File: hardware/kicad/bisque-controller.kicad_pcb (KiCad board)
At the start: 2 copper layers, 100 x 80 mm, 52 parts, among them J1 USB-C, J2 5V_IN, J3 TC_K, J4 SSR, J5 DISPLAY, J6 NAV_SW, J7 AUX, Q1 AO3400A, Q2 AO3400A, SW1 RESET, SW2 BOOT, U1 ESP32-S3-WROOM-1-N16R8, U2 AMS1117-3.3, U3 MAX31855KASA+, U4 USBLC6-2SC6

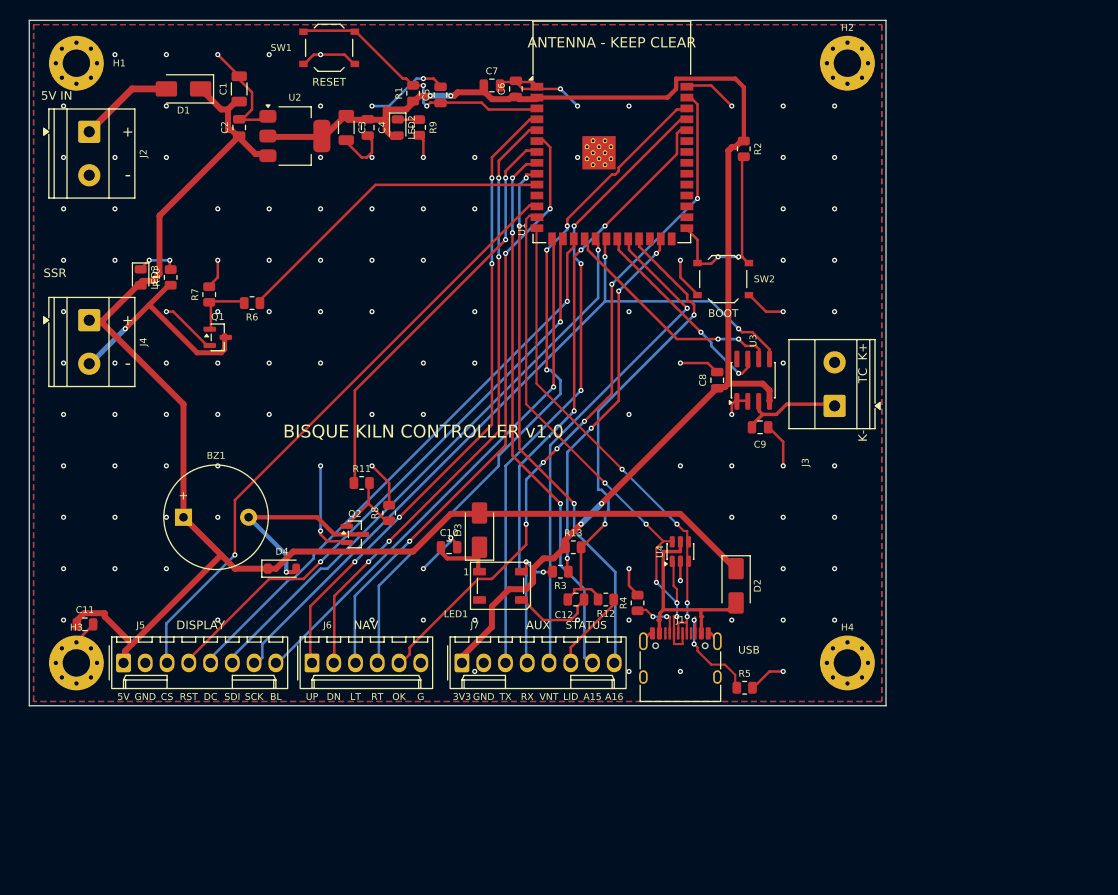
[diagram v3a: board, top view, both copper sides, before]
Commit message: wip(hw): rev B place and route — rung 2, still 27 unconnected
Full re-placement of all 141 footprints and a first end-to-end route of the
rev B board. Does NOT reach the 0-error/0-unconnected gate: 78 DRC violations,
27 unconnected pads, 9 nets the router could not finish. Spec 6.3's ladder was
worked in order and neither affordable rung closed it.

  rung 0 (100x100, 0805): 34 unroutable, 149 violations, 38 unconnected
  rung 1 (100x100, 0603): 23 unroutable,  84 violations, 32 unconnected
  rung 2 (125x100, 0603):  9 unroutable,  78 violations, 27 unconnected

Rung 3 (4-layer) is what the remaining failures point at — they are all short
local nets boxed in by neighbours' copper, i.e. short of routing layer, not of
board area — but that changes the stack-up and fab cost, so it is escalated
rather than started. See .superpowers/sdd/2026-08-11-pcb-rev-b/task-14-report.md.

Placement is now data, not 141 hand-typed coordinates: floorplan.py holds the
region rectangles, the pinned parts and a seed per part plus an overlap
legalizer; apply_floorplan.py writes the result into design.py; and
check_placement.py answers "does anything collide" from design.py in a second
instead of after a 20-minute route and fill. Final: 0 courtyard overlaps,
0 parts off-board.

Generator fixes this needed, none of which relax a rule:

- kicad_build.py had never been run. It crashed in add_zones (pcbnew.LSET
  takes no python list in KiCad 10) and its ref-relocation table still named
  C9, deleted with the MAX31855.
- Dropped the WROOM-1 antenna keepout fallback. The 1U has no PCB antenna;
  inventing a keep-out for it barred tracks from a third of the digital band
  and forfeited the band the module swap exists to reclaim.
- Made the opto barrier a *router* keepout as well as a pour keepout, with an
  allow_nets exemption for SSR*_A/B. Otherwise stitch_vias drops free GND vias
  inside the band; and forbidding vias via the KiCad rule area instead made it
  flag J4/J9's own pads as "items n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
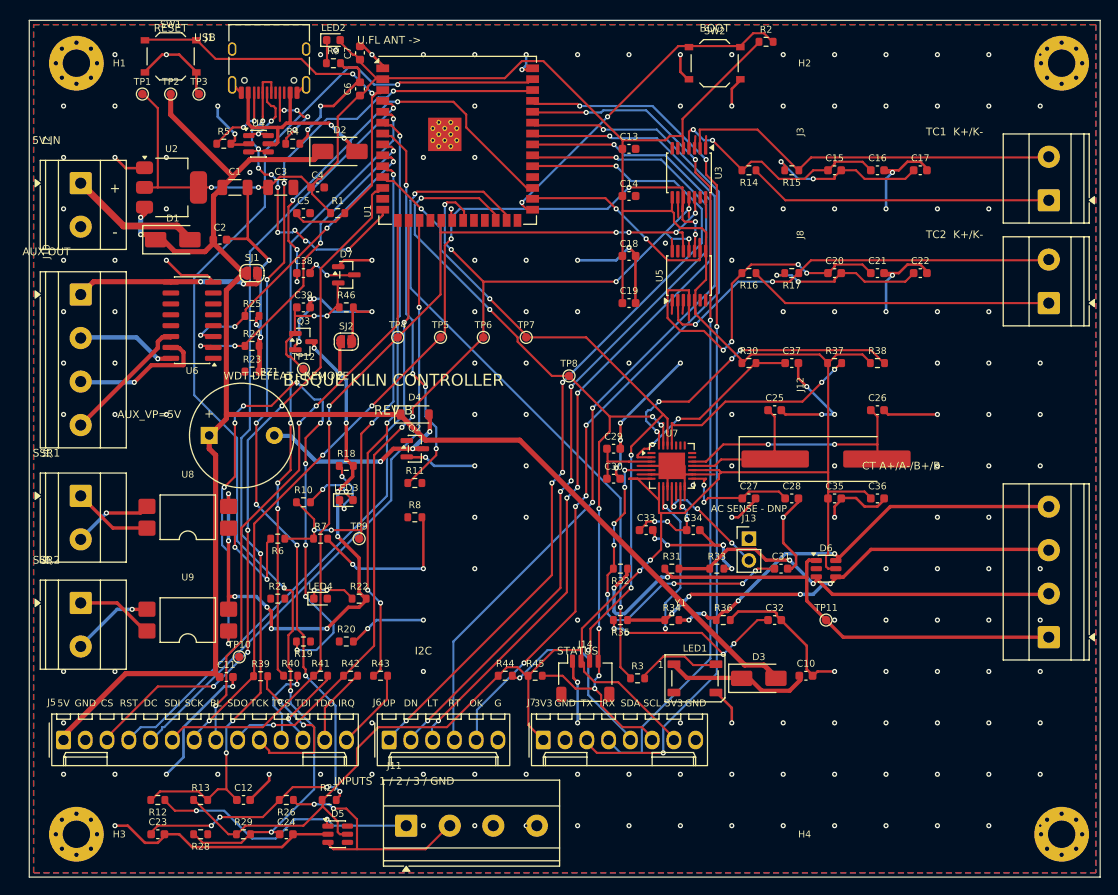
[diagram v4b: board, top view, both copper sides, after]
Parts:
- removed C8: 100nF, C_0805_2012Metric
- removed C9: 10nF, C_0805_2012Metric
- removed Q1: AO3400A, SOT-23
- added C13: 100nF, C_0603_1608Metric, F.Cu at (90.0, 35.0)
- added C14: 100nF, C_0603_1608Metric, F.Cu at (90.0, 40.5)
- added C15: 100nF, C_0603_1608Metric, F.Cu at (114.0, 37.5)
- added C16: 10nF, C_0603_1608Metric, F.Cu at (119.0, 37.5)
- added C17: 10nF, C_0603_1608Metric, F.Cu at (124.0, 37.5)
- added C18: 100nF, C_0603_1608Metric, F.Cu at (90.0, 47.5)
- added C19: 100nF, C_0603_1608Metric, F.Cu at (90.0, 53.0)
- added C20: 100nF, C_0603_1608Metric, F.Cu at (114.0, 49.5)
- added C21: 10nF, C_0603_1608Metric, F.Cu at (119.0, 49.5)
- added C22: 10nF, C_0603_1608Metric, F.Cu at (124.0, 49.5)
- added C23: 100nF, C_0603_1608Metric, F.Cu at (35.0, 115.0)
- added C24: 100nF, C_0603_1608Metric, F.Cu at (50.0, 115.0)
- added C25: 30pF, C_0603_1608Metric, F.Cu at (107.0, 65.5)
- added C26: 30pF, C_0603_1608Metric, F.Cu at (119.0, 65.5)
- added C27: 4.7uF, C_0603_1608Metric, F.Cu at (104.0, 75.8)
- added C28: 100nF, C_0603_1608Metric, F.Cu at (109.0, 75.8)
- added C29: 4.7uF, C_0603_1608Metric, F.Cu at (88.2, 70.0)
- added C30: 100nF, C_0603_1608Metric, F.Cu at (88.2, 73.5)
- added C31: 33nF, C_0603_1608Metric, F.Cu at (107.8, 84.0)
- added C32: 33nF, C_0603_1608Metric, F.Cu at (107.0, 90.0)
- added C33: 4.7uF, C_0603_1608Metric, F.Cu at (92.0, 79.5)
- added C34: 100nF, C_0603_1608Metric, F.Cu at (97.5, 79.5)
- added C35: 10uF, C_0603_1608Metric, F.Cu at (114.0, 75.8)
- added C36: 100nF, C_0603_1608Metric, F.Cu at (119.0, 75.8)
- added C37: 1uF, C_0603_1608Metric, F.Cu at (109.0, 60.0)
- added C38: 100nF, C_0603_1608Metric, F.Cu at (52.0, 49.5)
- added C39: 1uF, C_0603_1608Metric, F.Cu at (52.0, 53.5)
- added D5: SRV05-4, SOT-23-6, F.Cu at (56.0, 115.0)
- added D6: SRV05-4, SOT-23-6, F.Cu at (113.0, 84.0)
- added D7: BAT54S, SOT-23, F.Cu at (57.0, 49.7)
- added J10: AUX, TerminalBlock_Phoenix_MKDS-1,5-4-5.08_1x04_P5.08mm_Horizontal, F.Cu at (26.0, 52.0)
- added J11: INPUTS, TerminalBlock_Phoenix_MKDS-1,5-4-5.08_1x04_P5.08mm_Horizontal, F.Cu at (64.0, 114.0)
- added J12: CT, TerminalBlock_Phoenix_MKDS-1,5-4-5.08_1x04_P5.08mm_Horizontal, F.Cu at (139.0, 92.0)
- added J13: AC_SENSE_DNP, PinHeader_1x02_P2.54mm_Vertical, F.Cu at (104.0, 80.5)
- added J14: QWIIC, JST_SH_SM04B-SRSS-TB_1x04-1MP_P1.00mm_Horizontal, F.Cu at (84.9, 96.8)
- added J8: TC2_K, TerminalBlock_Phoenix_MKDS-1,5-2-5.08_1x02_P5.08mm_Horizontal, F.Cu at (139.0, 53.0)
- added J9: SSR2, TerminalBlock_Phoenix_MKDS-1,5-2-5.08_1x02_P5.08mm_Horizontal, F.Cu at (26.0, 88.0)
- added LED4: amber, LED_0603_1608Metric, F.Cu at (54.0, 87.5)
- added Q3: AO3400A, SOT-23, F.Cu at (52.0, 57.5)
- added R14: 100R 1%, R_0603_1608Metric, F.Cu at (104.0, 37.5)
- added R15: 100R 1%, R_0603_1608Metric, F.Cu at (109.0, 37.5)
- added R16: 100R 1%, R_0603_1608Metric, F.Cu at (104.0, 49.5)
- added R17: 100R 1%, R_0603_1608Metric, F.Cu at (109.0, 49.5)
- added R18: 0R, R_0603_1608Metric, F.Cu at (57.0, 72.0)
- added R19: 220R, R_0603_1608Metric, F.Cu at (52.0, 92.5)
- added R20: 10k, R_0603_1608Metric, F.Cu at (57.0, 92.5)
- added R21: 680R, R_0603_1608Metric, F.Cu at (49.0, 87.5)
- added R22: 0R, R_0603_1608Metric, F.Cu at (58.5, 87.5)
- added R23: 10k, R_0603_1608Metric, F.Cu at (46.0, 61.0)
- added R24: 10k, R_0603_1608Metric, F.Cu at (46.0, 58.0)
- added R25: 10k, R_0603_1608Metric, F.Cu at (46.0, 54.5)
- added R26: 1k, R_0603_1608Metric, F.Cu at (50.0, 111.0)
- added R27: 10k, R_0603_1608Metric, F.Cu at (55.0, 111.0)
- added R28: 1k, R_0603_1608Metric, F.Cu at (40.0, 115.0)
- added R29: 10k, R_0603_1608Metric, F.Cu at (45.0, 115.0)
- added R30: 10k, R_0603_1608Metric, F.Cu at (104.0, 60.0)
- added R31: 6R8, R_0603_1608Metric, F.Cu at (95.0, 84.0)
- added R32: 1k, R_0603_1608Metric, F.Cu at (89.0, 84.0)
- added R33: 1k, R_0603_1608Metric, F.Cu at (100.2, 84.0)
- added R34: 6R8, R_0603_1608Metric, F.Cu at (95.0, 90.0)
- added R35: 1k, R_0603_1608Metric, F.Cu at (89.0, 90.0)
- added R36: 1k, R_0603_1608Metric, F.Cu at (101.0, 90.0)
- added R37: 10k, R_0603_1608Metric, F.Cu at (114.0, 60.0)
- added R38: 10k, R_0603_1608Metric, F.Cu at (119.0, 60.0)
- added R39: 33, R_0603_1608Metric, F.Cu at (47.0, 96.5)
- added R40: 33, R_0603_1608Metric, F.Cu at (50.5, 96.5)
- added R41: 33, R_0603_1608Metric, F.Cu at (54.0, 96.5)
- added R42: 33, R_0603_1608Metric, F.Cu at (57.5, 96.5)
- added R43: 33, R_0603_1608Metric, F.Cu at (61.0, 96.5)
- added R44: 4.7k, R_0603_1608Metric, F.Cu at (75.5, 96.5)
- added R45: 4.7k, R_0603_1608Metric, F.Cu at (79.0, 96.5)
- added R46: 1M, R_0603_1608Metric, F.Cu at (57.0, 53.5)
- added SJ1: AUX_VP=5V, SolderJumper-2_P1.3mm_Open_RoundedPad1.0x1.5mm, F.Cu at (46.0, 49.5)
- added SJ2: WDT_DEFEAT, SolderJumper-2_P1.3mm_Open_RoundedPad1.0x1.5mm, F.Cu at (57.0, 57.5)
- added TP1: TP, TestPoint_Pad_D1.0mm, F.Cu at (33.2, 28.6)
- added TP10: TP, TestPoint_Pad_D1.0mm, F.Cu at (44.5, 94.3)
- added TP11: TP, TestPoint_Pad_D1.0mm, F.Cu at (113.0, 90.0)
- added TP12: TP, TestPoint_Pad_D1.0mm, F.Cu at (52.0, 60.7)
- added TP2: TP, TestPoint_Pad_D1.0mm, F.Cu at (36.5, 28.6)
- added TP3: TP, TestPoint_Pad_D1.0mm, F.Cu at (39.8, 28.6)
- added TP4: TP, TestPoint_Pad_D1.0mm, F.Cu at (63.0, 57.0)
- added TP5: TP, TestPoint_Pad_D1.0mm, F.Cu at (68.0, 57.0)
- added TP6: TP, TestPoint_Pad_D1.0mm, F.Cu at (73.0, 57.0)
- added TP7: TP, TestPoint_Pad_D1.0mm, F.Cu at (78.0, 57.0)
- added TP8: TP, TestPoint_Pad_D1.0mm, F.Cu at (83.0, 61.5)
- added TP9: TP, TestPoint_Pad_D1.0mm, F.Cu at (58.5, 80.5)
- added U5: MAX31856MUD+, TSSOP-14_4.4x5mm_P0.65mm, F.Cu at (97.0, 49.8)
- added U6: ULN2003A, SOIC-16_3.9x9.9mm_P1.27mm, F.Cu at (39.0, 55.0)
- added U7: ADE7953ACPZ, QFN-28-1EP_5x5mm_P0.5mm_EP3.1x3.1mm, F.Cu at (95.0, 72.0)
- added U8: LTV-817S-TA1-C, SMDIP-4_W9.53mm, F.Cu at (38.5, 78.0)
- added U9: LTV-817S-TA1-C, SMDIP-4_W9.53mm, F.Cu at (38.5, 90.0)
- added Y1: 3.579545MHz, Crystal_SMD_HC49-SD_HandSoldering, F.Cu at (113.0, 71.2)
- C10, C11, C12, C2, C4, C5, C6, C7: footprint C_0805_2012Metric -> C_0603_1608Metric
- J3: value TC_K -> TC1_K
- J4: value SSR -> SSR1
- J5: footprint Molex_KK-254_AE-6410-08A_1x08_P2.54mm_Vertical -> Molex_KK-254_AE-6410-14A_1x14_P2.54mm_Vertical
- LED2, LED3: footprint LED_0805_2012Metric -> LED_0603_1608Metric
- R1, R10, R11, R12, R13, R2, R3, R4, R5, R7, R8, R9: footprint R_0805_2012Metric -> R_0603_1608Metric
- R6: value 100R -> 220R; footprint R_0805_2012Metric -> R_0603_1608Metric
- U1: value ESP32-S3-WROOM-1-N16R8 -> ESP32-S3-WROOM-1U-N16R2; footprint ESP32-S3-WROOM-1 -> ESP32-S3-WROOM-1U
- U3: value MAX31855KASA+ -> MAX31856MUD+; footprint SOIC-8_3.9x4.9mm_P1.27mm -> TSSOP-14_4.4x5mm_P0.65mm
- moved R5 87.9 mm to (42.7, 34.4)
- moved J1 85.9 mm to (48.0, 24.4), turned to 180 degrees
- moved D2 68.6 mm to (56.2, 35.3), turned to 0 degrees
- moved U4 68.5 mm to (46.8, 34.4), turned to 0 degrees
- moved R4 67.0 mm to (50.8, 34.4), turned to 0 degrees
- moved R12 57.3 mm to (35.0, 111.0)
- moved R13 52.6 mm to (40.0, 111.0)
- moved C12 45.3 mm to (45.0, 111.0)
- moved C10 44.3 mm to (110.7, 96.5)
- moved D3 36.9 mm to (105.2, 96.8), turned to 0 degrees
- moved LED3 35.4 mm to (57.0, 76.0), turned to 0 degrees
- moved J3 34.7 mm to (139.0, 41.0)
- moved H4 32.0 mm to (140.5, 115.0)
- moved R7 31.3 mm to (54.0, 80.5), turned to 0 degrees
- moved R10 30.5 mm to (52.0, 76.2), turned to 0 degrees
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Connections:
- C12 pad 1: LID_SW -> IN1
- J3 pad 1: TC_P -> TC1_P
- J3 pad 2: GND -> TC1_N
- J4 pad 1: +5V -> SSR1_A
- J4 pad 2: SSR_OUT -> SSR1_B
- J7 pad 5: VENT -> I2C_SDA
- J7 pad 6: LID_IN -> I2C_SCL
- J7 pad 7: AUX_A -> +3V3
- J7 pad 8: AUX_B -> GND
- LED3 pad 1: LEDS_K -> SSR1_IND_K
- LED3 pad 2: +5V -> SSR1_IND_A
- R10 pad 1: SSR_OUT -> SSR1_CTRL
- R10 pad 2: LEDS_K -> SSR1_IND_A
- R12 pad 1: LID_IN -> IN1_RAW
- R12 pad 2: LID_SW -> IN1
- R13 pad 2: LID_SW -> IN1
- R6 pad 1: SSR_CTRL -> SSR1_CTRL
- R6 pad 2: SSR_GATE -> SSR1_LED_A
- R7 pad 1: SSR_GATE -> SSR1_CTRL
- U1 pad 10: SSR_CTRL -> SSR1_CTRL
- U1 pad 11: (no net) -> I2C_SDA
- U1 pad 18: TC_CS -> TC1_CS
- U1 pad 22: VENT -> AUX1
- U1 pad 23: LID_SW -> SSR2_CTRL
- U1 pad 24: (no net) -> I2C_SCL
- U1 pad 28: (no net) -> TC2_CS
- U1 pad 29: (no net) -> WDT_KICK
- U1 pad 31: (no net) -> BTN_UP
- U1 pad 32: (no net) -> BTN_DOWN
- U1 pad 33: (no net) -> BTN_LEFT
- U1 pad 34: (no net) -> BTN_RIGHT
- U1 pad 35: (no net) -> BTN_SEL
- U1 pad 38: BTN_RIGHT -> IN2
- U1 pad 39: BTN_SEL -> IN3
- U1 pad 4: BTN_UP -> IN1
- U1 pad 5: BTN_DOWN -> T_CS
- U1 pad 6: BTN_LEFT -> T_IRQ
- U1 pad 8: AUX_A -> AUX2
- U1 pad 9: AUX_B -> AUX3
- U3 pad 2: GND -> TC1_N
- U3 pad 3: TC_P -> TC1_N_F
- U3 pad 4: +3V3 -> TC1_P_F
- U3 pad 5: SPI_SCLK -> +3V3
- U3 pad 6: TC_CS -> (no net)
- U3 pad 7: SPI_MISO -> (no net)
- U3 pad 8: (no net) -> +3V3
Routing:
- net GND: track 146.5 -> 387.6 mm, vias 116 -> 193
- net +3V3: track 157.5 -> 361.9 mm
- net IN3: track 0.00 -> 139.1 mm, vias 0 -> 4
- net IN2: track 0.00 -> 136.6 mm, vias 0 -> 11
- net I2C_SCL: track 0.00 -> 105.4 mm, vias 0 -> 8
- net I2C_SDA: track 0.00 -> 104.7 mm, vias 0 -> 6
- net IN1: track 0.00 -> 103.2 mm, vias 0 -> 4
- net SPI_MISO: track 23.9 -> 118.6 mm, vias 2 -> 8
- net SSR2_LED_A: track 0.00 -> 77.2 mm, vias 0 -> 10
- net SSR_EN: track 0.00 -> 73.4 mm, vias 0 -> 11
- net T_CS: track 0.00 -> 72.7 mm, vias 0 -> 4
- net T_IRQ: track 0.00 -> 68.3 mm, vias 0 -> 4
- net CTA_P: track 0.00 -> 67.0 mm, vias 0 -> 2
- net AUX_A: track 64.3 -> 0.00 mm, vias 3 -> 0
- net AUX_B: track 63.5 -> 0.00 mm, vias 3 -> 0
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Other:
- board size 100 x 80 mm -> 125 x 100 mm
- board text added: "AC SENSE - DNP"
- board text added: "AUX OUT"
- board text added: "AUX_VP=5V"
- board text added: "BISQUE KILN CONTROLLER"
- board text added: "CT A+/A-/B+/B-"
- board text added: "I2C"
- board text added: "INPUTS 1 / 2 / 3 / GND"
- board text added: "IRQ"
- board text added: "REV B"
- board text added: "SCL"
- board text added: "SDA"
- board text added: "SDO"
- board text added: "SSR1"
- board text added: "SSR2"
- board text added: "TC1 K+/K-"
- board text added: "TC2 K+/K-"
- board text added: "TCK"
- board text added: "TCS"
- board text added: "TDI"
- board text added: "TDO"
- board text added: "U.FL ANT ->"
- board text added: "WDT DEFEAT - REMOVE"
- board text removed: "A15"
- board text removed: "A16"
- board text removed: "ANTENNA - KEEP CLEAR"
- board text removed: "AUX"
- board text removed: "BISQUE KILN CONTROLLER v1.0"
- board text removed: "DISPLAY"
- board text removed: "K-"
- board text removed: "LID"
- board text removed: "NAV"
- board text removed: "SSR"
- board text removed: "TC K+"
- board text removed: "VNT"
